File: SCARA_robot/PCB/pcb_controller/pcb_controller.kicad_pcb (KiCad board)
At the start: 2 copper layers, 100 x 100 mm, 96 parts, among them J1 Barrel_Jack_Switch, J10 interface, J11 Conn_01x07_Socket, J15 Conn_01x04_Pin_STEPPER_B, J16 Conn_01x04_Pin_STEPPER_C, J17 Conn_01x02_Pin, J18 Conn_01x04_Pin_STEPPER_C, J19 Conn_01x04_Pin_STEPPER_C, J2 Conn_01x04_Pin_STEPPER_A, J20 Conn_01x04_Pin_STEPPER_C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

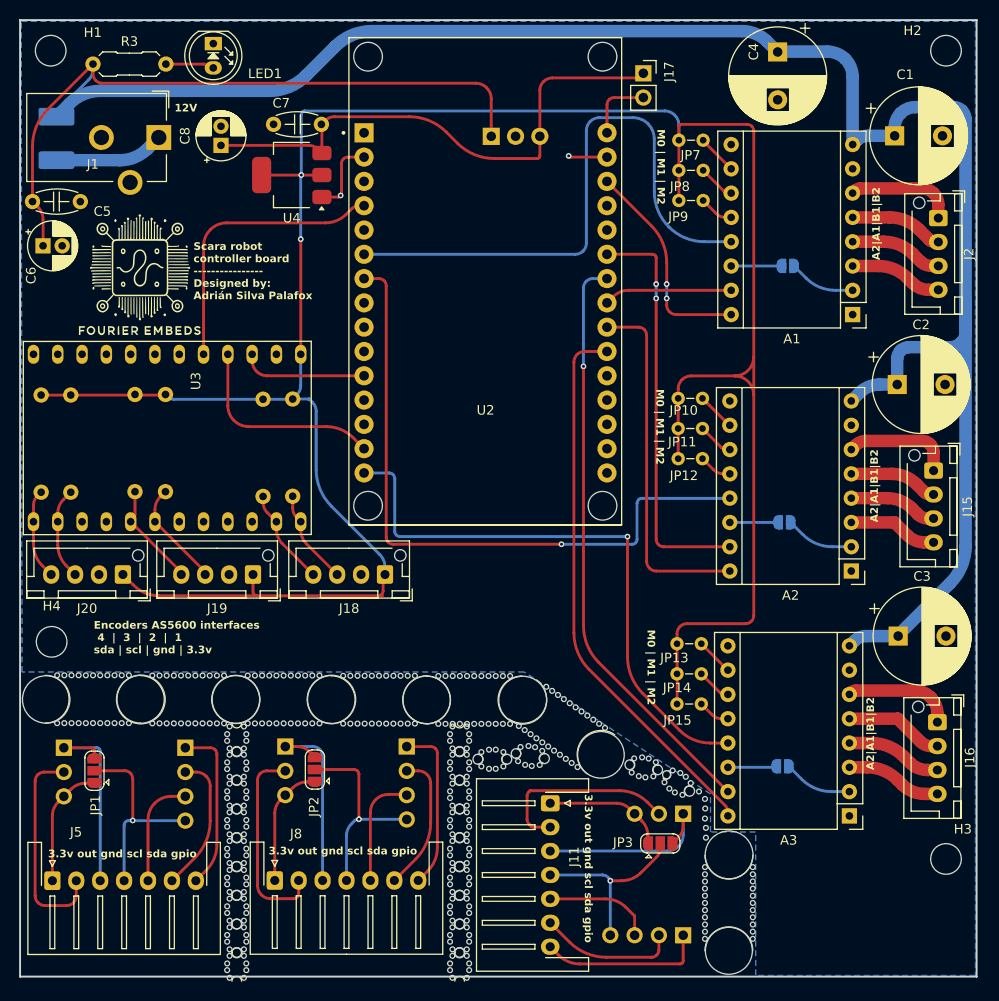
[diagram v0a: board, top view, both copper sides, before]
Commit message: pcb finalizada y ordenada
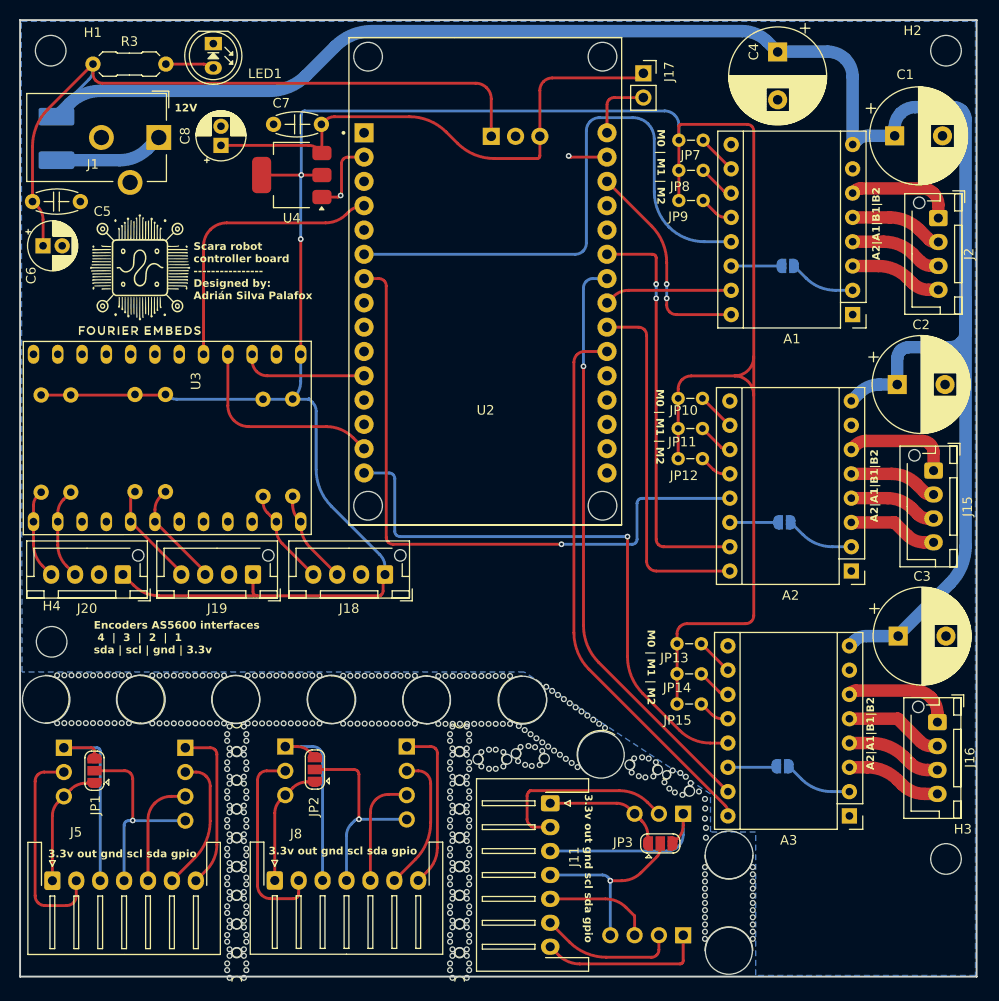
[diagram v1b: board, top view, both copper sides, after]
